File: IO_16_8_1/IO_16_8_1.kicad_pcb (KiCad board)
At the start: 2 copper layers, 228 parts, among them J1 Conn_01x06, J10 Conn_01x06, J11 Conn_01x06, J2 nmount JST 1mm QWIIC, J3 nmount SW Debug, J4 USB_C_Receptacle_USB2.0, J5 Conn_01x06, J6 Conn_01x06, J7 Conn_01x06, J8 Conn_01x06, J9 Conn_01x06, Q1 2N7002, Q10 2N7002, Q11 2N7002, Q12 2N7002, Q13 AO3400A, Q14 AO3400A, Q15 AO3400A, Q16 AO3400A, Q17 2N7002, Q18 2N7002, Q19 2N7002, Q2 2N7002, Q20 2N7002, Q21 2N7002, Q22 2N7002, Q23 2N7002, Q24 2N7002, Q25 IRLR3410, Q26 IRLR3410, Q27 IRLR3410, Q28 IRLR3410, Q29 IRLR3410, Q3 2N7002, Q30 IRLR3410, Q31 IRLR3410, Q32 IRLR3410, Q4 2N7002, Q5 2N7002, Q6 2N7002, Q7 2N7002, Q8 2N7002, Q9 2N7002, SW1 Reset, SW2 Boot, SW3 SW_DIP_x04, U1 ADM3483, U2 W25Q32JVSS, U3 RP2040, U4 LMV321, U5 SN74AHCT1G125, U6 AP2112K-3.3, Y1 12MHz,18pF

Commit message: placed out
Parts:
- added REF**: MountingHole_5.5mm_Pinball, IO_16_8_1:MountingHole_5.5mm_Pinball, F.Cu at (80.0, 134.0)
- added REF**: MountingHole_5.5mm_Pinball, IO_16_8_1:MountingHole_5.5mm_Pinball, F.Cu at (170.0, 134.0)
- added REF**: MountingHole_5.5mm_Pinball, IO_16_8_1:MountingHole_5.5mm_Pinball, F.Cu at (170.0, 44.0)
- added REF**: MountingHole_5.5mm_Pinball, IO_16_8_1:MountingHole_5.5mm_Pinball, F.Cu at (80.0, 44.0)
- moved C31 264.0 mm to (149.8, 154.0)
- moved C32 264.0 mm to (123.9, 174.1)
- moved C33 264.0 mm to (123.9, 176.6)
- moved C34 264.0 mm to (150.7, 149.5)
- moved C41 264.0 mm to (146.0, 166.5)
- moved C43 264.0 mm to (154.9, 157.6)
- moved C44 264.0 mm to (123.9, 179.1)
- moved Q1 264.0 mm to (104.8, 180.7)
- moved Q10 264.0 mm to (95.0, 185.2)
- moved Q11 264.0 mm to (130.4, 161.2)
- moved Q12 264.0 mm to (114.5, 180.7)
- moved Q13 264.0 mm to (151.1, 146.0)
- moved Q15 264.0 mm to (104.8, 176.3)
- moved Q16 264.0 mm to (99.9, 180.7)
- moved Q18 264.0 mm to (125.5, 165.6)
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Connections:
- R79 pad 1: /Out_1 -> /Out_3
- R81 pad 1: /Out_3 -> /Out_1
- R82 pad 1: /Out_1 -> /Out_3
- R84 pad 1: /Out_3 -> /Out_1
- R85 pad 1: /Out_4 -> /Out_6
- R87 pad 1: /Out_6 -> /Out_4
- R88 pad 1: /Out_4 -> /Out_6
- R90 pad 1: /Out_6 -> /Out_4
- R91 pad 1: /Out_7 -> /Out_8
- R92 pad 1: /Out_8 -> /Out_7
- R93 pad 1: /Out_7 -> /Out_8
- R94 pad 1: /Out_8 -> /Out_7
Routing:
- net +48V: track 0.00 -> 207.3 mm
- net GNDPWR: track 0.00 -> 72.9 mm
- net /OUT8/48V_IN: track 0.00 -> 17.1 mm
- net Net-(C55-Pad1): track 0.00 -> 13.5 mm
- net Net-(C54-Pad1): track 0.00 -> 13.5 mm
- net Net-(C50-Pad1): track 0.00 -> 12.3 mm
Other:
- board outline added: 100 x 100 mm

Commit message: placed logic
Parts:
- moved R5 179.6 mm to (98.0, 55.5)
- moved D1 177.6 mm to (93.0, 56.0)
- moved C3 175.3 mm to (103.5, 62.0)
- moved R4 173.4 mm to (98.5, 58.0)
- moved C1 172.8 mm to (100.0, 66.0)
- moved C23 172.7 mm to (111.0, 56.5), turned to -90 degrees
- moved R2 171.9 mm to (95.5, 67.0)
- moved R3 170.9 mm to (98.5, 62.0)
- moved C2 170.8 mm to (103.5, 65.0)
- moved C21 170.3 mm to (165.6, -14.0)
- moved C10 170.3 mm to (135.3, 22.1)
- moved C15 170.3 mm to (155.9, -8.17)
- moved C19 170.3 mm to (158.7, -3.15)
- moved C9 170.3 mm to (98.0, 27.8)
- moved C12 170.3 mm to (137.2, 17.1)
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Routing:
- net +48V: track 207.3 -> 321.1 mm
- net GNDPWR: track 72.9 -> 104.4 mm
- net Net-(C46-Pad1): track 0.00 -> 20.6 mm
- net Net-(C51-Pad1): track 0.00 -> 20.4 mm
- net Net-(C47-Pad1): track 0.00 -> 20.2 mm
- net Net-(C52-Pad1): track 0.00 -> 20.0 mm
- net Net-(C48-Pad1): track 0.00 -> 19.7 mm
- net Net-(C50-Pad1): track 12.3 -> 20.8 mm
- net Net-(C54-Pad1): track 13.5 -> 20.7 mm
- net Net-(C55-Pad1): track 13.5 -> 20.3 mm
- net /OUT8/48V_IN: track 17.1 -> 14.7 mm

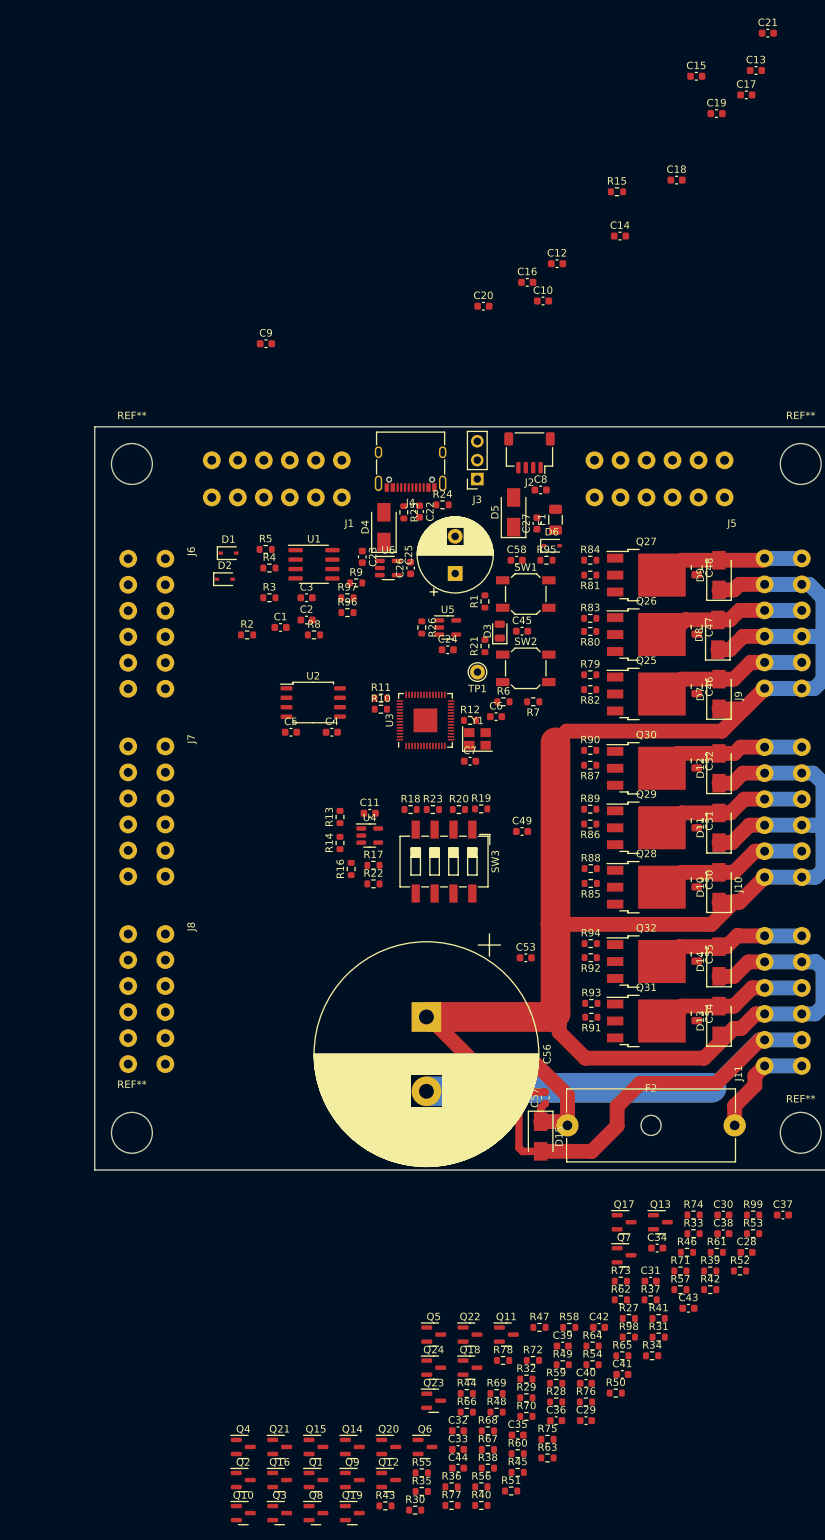
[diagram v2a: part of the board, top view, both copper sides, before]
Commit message: smaller Cs
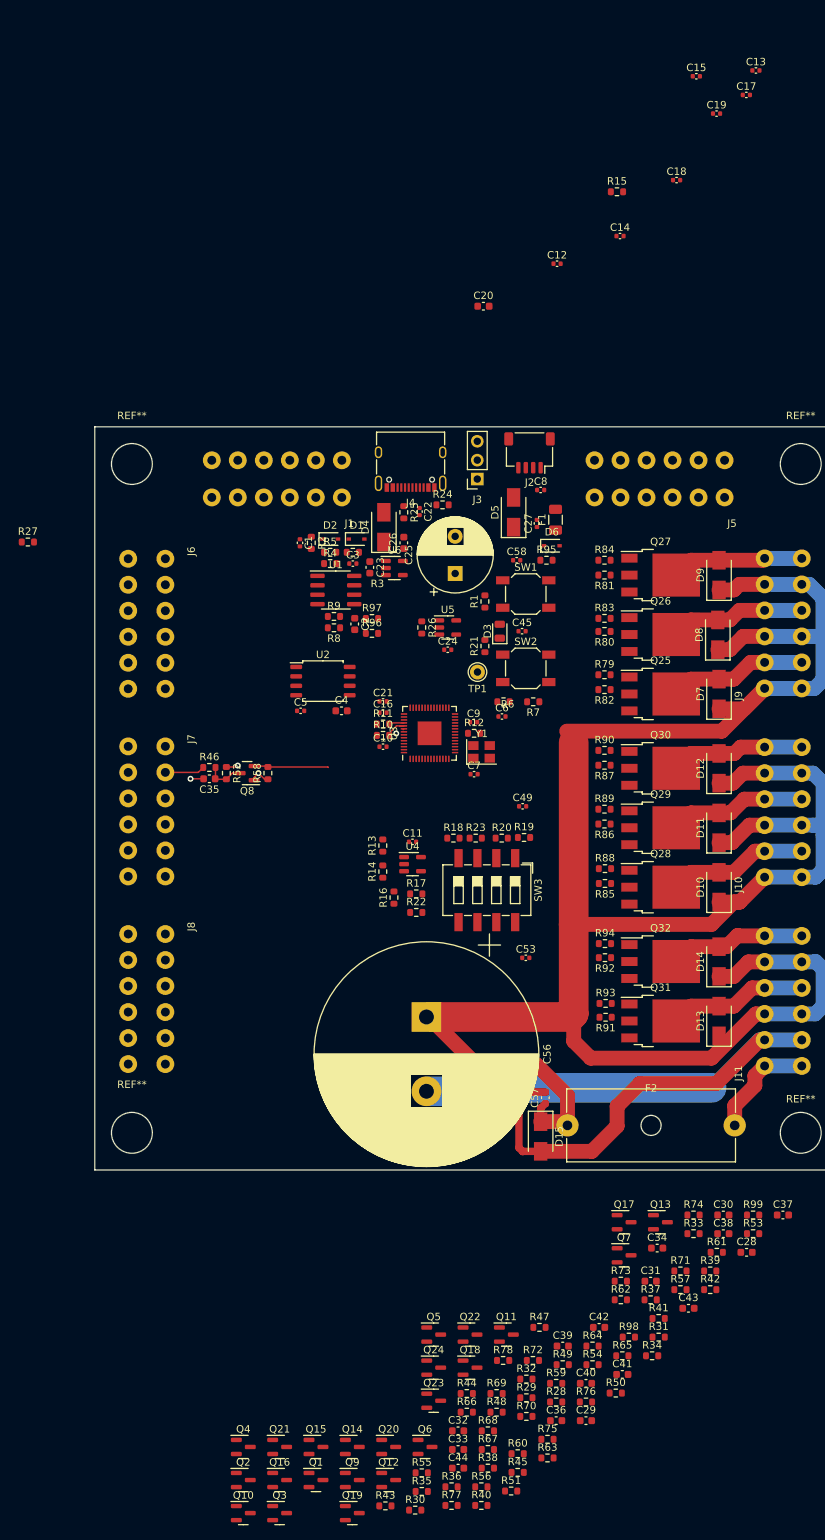
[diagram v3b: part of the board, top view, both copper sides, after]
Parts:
- removed C46, C47, C48, C50, C51, C52, C54, C55: 470p 500V, Capacitor_SMD:C_0805_2012Metric
- C1, C10, C11, C12, C13, C14, C15, C17, C18, C19, C22, C24, C27, C3, C45, C49, C5, C53, C58, C6, C7, C8, C9: footprint Capacitor_SMD:C_0603_1608Metric -> Capacitor_SMD:C_0402_1005Metric
- C16, C21: value 10u -> 1u; footprint Capacitor_SMD:C_0603_1608Metric -> Capacitor_SMD:C_0402_1005Metric
- moved R27 132.1 mm to (66.0, 54.5)
- moved C21 103.8 mm to (113.8, 75.9)
- moved Q8 100.0 mm to (95.5, 85.6), turned to 180 degrees
- moved C35 97.6 mm to (90.4, 86.4), turned to 180 degrees
- moved R52 96.3 mm to (92.7, 85.6), turned to -90 degrees
- moved R46 91.6 mm to (90.4, 84.8)
- moved R58 84.9 mm to (98.3, 85.6), turned to 90 degrees
- moved C10 63.7 mm to (113.8, 82.0)
- moved C16 61.1 mm to (113.8, 77.5)
- moved C9 58.1 mm to (126.0, 78.7)
- moved D1 17.3 mm to (110.2, 54.1)
- moved D2 15.2 mm to (106.7, 54.1)
- moved R2 15.1 mm to (104.1, 54.6), turned to -90 degrees
- moved R3 12.8 mm to (109.7, 55.9), turned to 180 degrees
- moved C1 11.7 mm to (102.6, 54.6), turned to -90 degrees
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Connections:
- C1 pad 1: Net-(C1-Pad1) -> Net-(J1-Pad3)
- J1 pad 3: Net-(C1-Pad1) -> Net-(J1-Pad3)
- J1 pad 4: Net-(D1-Pad1) -> GND
- J1 pad 5: Net-(D2-Pad1) -> GND
- J1 pad 6: Net-(C1-Pad1) -> GND
- R2 pad 1: Net-(C1-Pad1) -> Net-(J1-Pad3)
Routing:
- net /In_8: track 0.00 -> 10.1 mm
- net Net-(J7-Pad2): track 0.00 -> 5.37 mm
- net Net-(C35-Pad1): track 0.00 -> 5.28 mm
- net +48V: track 321.1 -> 317.8 mm
- net +3V3: track 0.00 -> 2.97 mm, vias 0 -> 2
- net Net-(R10-Pad2): track 0.00 -> 2.60 mm
- net Net-(R11-Pad2): track 0.00 -> 2.06 mm
- net Net-(D8-Pad2): track 20.2 -> 18.2 mm
- net Net-(D9-Pad2): track 19.7 -> 17.8 mm
- net Net-(D7-Pad2): track 20.6 -> 18.7 mm
- net Net-(D14-Pad2): track 20.3 -> 18.4 mm
- net Net-(D11-Pad2): track 20.4 -> 18.5 mm
- net Net-(D13-Pad2): track 20.7 -> 18.7 mm
- net Net-(D10-Pad2): track 20.8 -> 18.9 mm
- net GND: track 0.00 -> 1.77 mm, vias 0 -> 1
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
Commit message: 1/2 routed
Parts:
- removed C18: 100n, Capacitor_SMD:C_0402_1005Metric
- D4: value 3A SMA -> 1A; footprint Diode_SMD:D_SMA -> Diode_SMD:D_SOD-323
- R10, R11, R12, R16, R20, R3, R5, R6: footprint Resistor_SMD:R_0603_1608Metric -> Resistor_SMD:R_0402_1005Metric
- moved C13 105.0 mm to (114.0, 83.4), turned to 180 degrees
- moved C15 96.5 mm to (126.2, 83.7)
- moved C17 92.4 mm to (125.2, 78.8)
- moved C19 87.4 mm to (119.4, 74.9), turned to 90 degrees
- moved C14 79.8 mm to (121.4, 89.4)
- moved R15 71.8 mm to (126.2, 76.5), turned to -90 degrees
- moved C12 64.7 mm to (115.3, 78.0), turned to 90 degrees
- moved C20 53.8 mm to (124.7, 76.5), turned to 90 degrees
- moved J3 44.4 mm to (126.3, 90.4), turned to 90 degrees
- moved R96 23.6 mm to (124.7, 46.7), turned to 180 degrees
- moved SW1 22.1 mm to (133.1, 83.6), turned to -90 degrees
- moved C24 21.2 mm to (139.2, 55.9), turned to 180 degrees
- moved D4 20.5 mm to (134.2, 49.7)
- moved R97 20.5 mm to (124.7, 48.5), turned to 180 degrees
- moved C23 20.2 mm to (132.1, 55.6), turned to 180 degrees
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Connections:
- R79 pad 1: /Out_3 -> /Out_6
- R80 pad 1: /Out_2 -> /Out_7
- R81 pad 1: /Out_1 -> /Out_8
- R82 pad 1: /Out_3 -> /Out_6
- R83 pad 1: /Out_2 -> /Out_7
- R84 pad 1: /Out_1 -> /Out_8
- R85 pad 1: /Out_6 -> /Out_3
- R86 pad 1: /Out_5 -> /Out_4
- R87 pad 1: /Out_4 -> /Out_5
- R88 pad 1: /Out_6 -> /Out_3
- R89 pad 1: /Out_5 -> /Out_4
- R90 pad 1: /Out_4 -> /Out_5
- R91 pad 1: /Out_8 -> /Out_1
- R92 pad 1: /Out_7 -> /Out_2
- R93 pad 1: /Out_8 -> /Out_1
- R94 pad 1: /Out_7 -> /Out_2
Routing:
- net GNDPWR: track 104.4 -> 214.6 mm, vias 0 -> 9
- net +3V3: track 2.97 -> 74.8 mm, vias 2 -> 6
- net GND: track 1.77 -> 57.2 mm
- net /Out_1: track 0.00 -> 48.3 mm, vias 0 -> 2
- net /5V_IN: track 0.00 -> 43.1 mm
- net /Out_2: track 0.00 -> 41.5 mm, vias 0 -> 2
- net /Out_8: track 0.00 -> 38.0 mm, vias 0 -> 2
- net /Out_Special: track 0.00 -> 34.9 mm, vias 0 -> 2
- net /Q_nCS: track 0.00 -> 33.9 mm, vias 0 -> 3
- net /USB_D+: track 0.00 -> 32.9 mm
- net /USB_D-: track 0.00 -> 32.7 mm
- net /Out_7: track 0.00 -> 31.1 mm, vias 0 -> 2
- net /485_DE: track 0.00 -> 30.8 mm
- net /Out_3: track 0.00 -> 30.6 mm, vias 0 -> 2
- net /Out_6: track 0.00 -> 25.1 mm, vias 0 -> 2
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- added copper zone on B.Cu, net GNDPWR

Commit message: placed
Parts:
- moved R40 125.8 mm to (100.3, 61.2), turned to 90 degrees
- moved Q1 123.4 mm to (96.0, 57.6), turned to 180 degrees
- moved C29 121.6 mm to (90.9, 61.9), turned to 180 degrees
- moved Q3 120.5 mm to (97.5, 64.7), turned to 180 degrees
- moved R30 120.4 mm to (90.9, 67.5)
- moved R35 120.3 mm to (93.2, 64.7), turned to -90 degrees
- moved Q2 119.6 mm to (97.5, 61.2), turned to 180 degrees
- moved R28 119.1 mm to (90.9, 60.4)
- moved R34 117.5 mm to (93.2, 61.2), turned to -90 degrees
- moved R36 117.2 mm to (93.2, 68.3), turned to -90 degrees
- moved C28 116.3 mm to (90.9, 58.6), turned to 180 degrees
- moved R29 113.8 mm to (90.9, 64.0)
- moved R43 113.7 mm to (98.5, 71.6), turned to 90 degrees
- moved R39 111.8 mm to (98.8, 57.6), turned to 90 degrees
- moved R98 109.9 mm to (94.7, 64.7), turned to -90 degrees
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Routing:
- net /In_1: track 0.00 -> 30.3 mm
- net /In_2: track 0.00 -> 27.5 mm
- net /In_3: track 0.00 -> 25.2 mm
- net GND: track 57.2 -> 81.0 mm, vias 1 -> 3
- net /In_13: track 3.69 -> 26.9 mm
- net Net-(C41-Pad1): track 0.00 -> 20.6 mm
- net /In_4: track 0.00 -> 20.5 mm
- net /In_5: track 0.00 -> 17.7 mm
- net /In_6: track 0.00 -> 17.1 mm
- net /In_11: track 1.73 -> 17.9 mm
- net /In_7: track 0.00 -> 14.9 mm
- net /In_12: track 3.16 -> 17.5 mm
- net /In_10: track 1.49 -> 15.6 mm
- net /In_9: track 0.00 -> 13.7 mm
- net +3V3: track 74.8 -> 84.9 mm, vias 6 -> 7
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
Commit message: routed
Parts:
- moved R14 21.3 mm to (130.3, 103.9), turned to 180 degrees
- moved R16 20.5 mm to (129.8, 105.8), turned to 0 degrees
- moved R17 19.6 mm to (130.6, 94.5), turned to 90 degrees
- moved R22 19.1 mm to (128.0, 93.7), turned to 180 degrees
- moved R13 18.9 mm to (130.3, 102.4), turned to 0 degrees
- moved U4 17.8 mm to (130.6, 99.6), turned to 90 degrees
- moved C11 14.8 mm to (129.8, 97.0), turned to 0 degrees
- moved R19 14.6 mm to (115.1, 102.1), turned to 180 degrees
- moved R20 14.6 mm to (115.8, 106.2), turned to 90 degrees
- moved C27 8.79 mm to (129.5, 57.1), turned to -90 degrees
- moved R23 6.93 mm to (115.1, 98.0)
- moved R18 6.63 mm to (115.1, 100.3), turned to 180 degrees
- moved C5 5.02 mm to (110.7, 68.6), turned to 180 degrees
- moved R97 2.81 mm to (117.3, 48.0), turned to 0 degrees
- moved R79 2.00 mm to (143.6, 74.4), turned to 180 degrees
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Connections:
- net Net-(C10-Pad1) renamed /1V1
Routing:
- net +3V3: track 84.9 -> 326.6 mm, vias 7 -> 33
- net +5V: track 11.2 -> 194.3 mm, vias 2 -> 22
- net GND: track 81.0 -> 224.3 mm, vias 3 -> 66
- net /In_16: track 3.31 -> 68.3 mm, vias 1 -> 2
- net /In_15: track 1.34 -> 60.7 mm, vias 1 -> 2
- net /In_14: track 3.48 -> 55.8 mm, vias 1 -> 2
- net /3V3A: track 2.80 -> 42.8 mm, vias 0 -> 2
- net GNDPWR: track 214.6 -> 252.7 mm, vias 9 -> 54
- net /485_RX: track 18.5 -> 55.0 mm, vias 0 -> 2
- net /485_TX: track 17.1 -> 53.4 mm, vias 0 -> 2
- net /1V1: track 9.52 -> 35.1 mm, vias 0 -> 3
- net Net-(R16-Pad1): track 0.00 -> 23.1 mm
- net Net-(D2-Pad1): track 5.00 -> 27.8 mm, vias 0 -> 2
- net /V_addr: track 11.0 -> 33.1 mm, vias 1 -> 2
- net Net-(D1-Pad1): track 5.00 -> 27.1 mm, vias 0 -> 2
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
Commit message: routed
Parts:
- added TP2: TP_GND, Connector_Pin:Pin_D1.0mm_L10.0mm, F.Cu at (123.7, 40.9)
- SW3: value SW_DIP_x04 -> ADDRESS
- moved R25 0.51 mm to (127.8, 50.0)
- moved REF** 0.48 mm to (80.0, 134.0)
- moved REF** 0.48 mm to (80.0, 44.0)
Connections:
- net /LED_Strip renamed /Out_S
- net Net-(C1-Pad1) renamed /SHD
- net Net-(D1-Pad1) renamed /A
- net Net-(D2-Pad1) renamed /B
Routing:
- net GND: track 224.3 -> 235.1 mm, vias 66 -> 286
- net Net-(D4-Pad2): track 1.85 -> 9.22 mm, vias 0 -> 2
- net +3V3: track 326.6 -> 333.3 mm, vias 33 -> 32
- net +5V: track 194.3 -> 200.5 mm
- net GNDPWR: track 252.7 -> 258.3 mm
- net /In_7: track 18.8 -> 22.7 mm
- net Net-(Q16-Pad1): track 2.00 -> 5.10 mm
- net Net-(D3-Pad2): track 2.38 -> 5.25 mm
- net /USB_D-: track 33.2 -> 36.1 mm
- net /USB_D+: track 33.4 -> 36.1 mm
- net /Out_4: track 25.9 -> 28.6 mm
- net Net-(Q29-Pad1): track 0.00 -> 2.62 mm
- net /In_16: track 68.3 -> 70.4 mm
- net /In_8: track 17.9 -> 19.9 mm
- net Net-(R17-Pad2): track 0.00 -> 1.74 mm
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- added copper zone on B.Cu, net GND
- added copper zone on F.Cu, net GND
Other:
- board text added: "1"
- board text added: "10"
- board text added: "11"
- board text added: "12"
- board text added: "13"
- board text added: "14"
- board text added: "15"
- board text added: "16"
- board text added: "17"
- board text added: "18"
- board text added: "19"
- board text added: "2"
- board text added: "20"
- board text added: "21"
- board text added: "22"
- board text added: "23"
- board text added: "24"
- board text added: "25"
- board text added: "3"
- board text added: "4"
- board text added: "5"
- board text added: "5V"
- board text added: "5_IN"
- board text added: "6"
- board text added: "7"
- board text added: "8"
- board text added: "9"
- board text added: "A"
- board text added: "B"
- board text added: "G"
- board text added: "G_IN"
- board text added: "HV"
- board text added: "HV_IN"
- board text added: "PPUC IO_16_8_1"
- board text added: "SHD"
- board text added: "T6A"

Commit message: v010review
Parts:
- moved R26 1.02 mm to (135.1, 57.9)
- moved U5 1.02 mm to (138.2, 58.2)
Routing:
- net GNDPWR: track 258.3 -> 250.8 mm, vias 54 -> 51
- net GND: track 235.1 -> 234.0 mm, vias 286 -> 287
- net /Out_8: track 43.5 -> 42.4 mm
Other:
- board text added: "PPUC"
